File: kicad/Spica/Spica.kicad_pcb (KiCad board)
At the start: 2 copper layers, 61 x 61 mm, 13 parts, among them IC1 TA48033S, M1 Motor_DC, M2 Motor_DC, SW1 SW_SPDT, U1 ESP32-DEVKITC-32D, U2 DRV8835-akizuki, U3 HC-SR04, U4 AE-XCL102D503CR-G

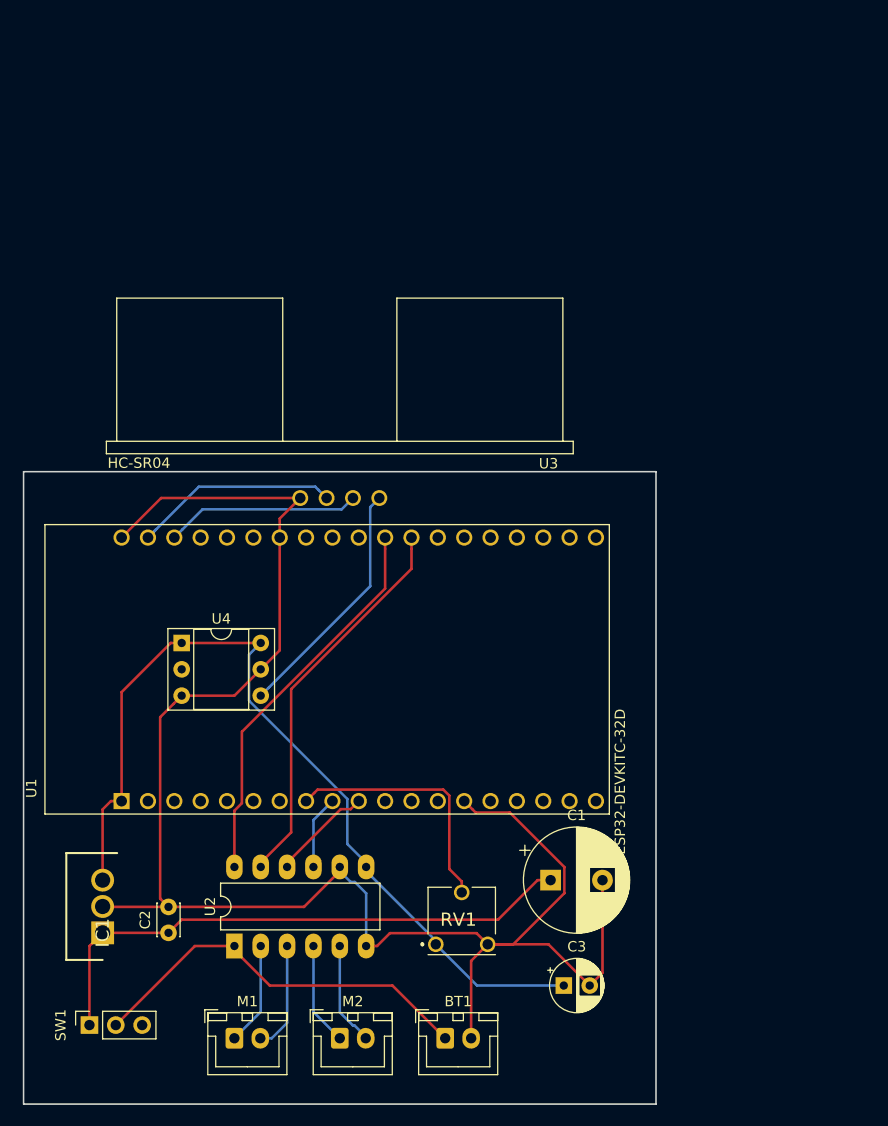
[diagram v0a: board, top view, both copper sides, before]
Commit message: Add surface GND
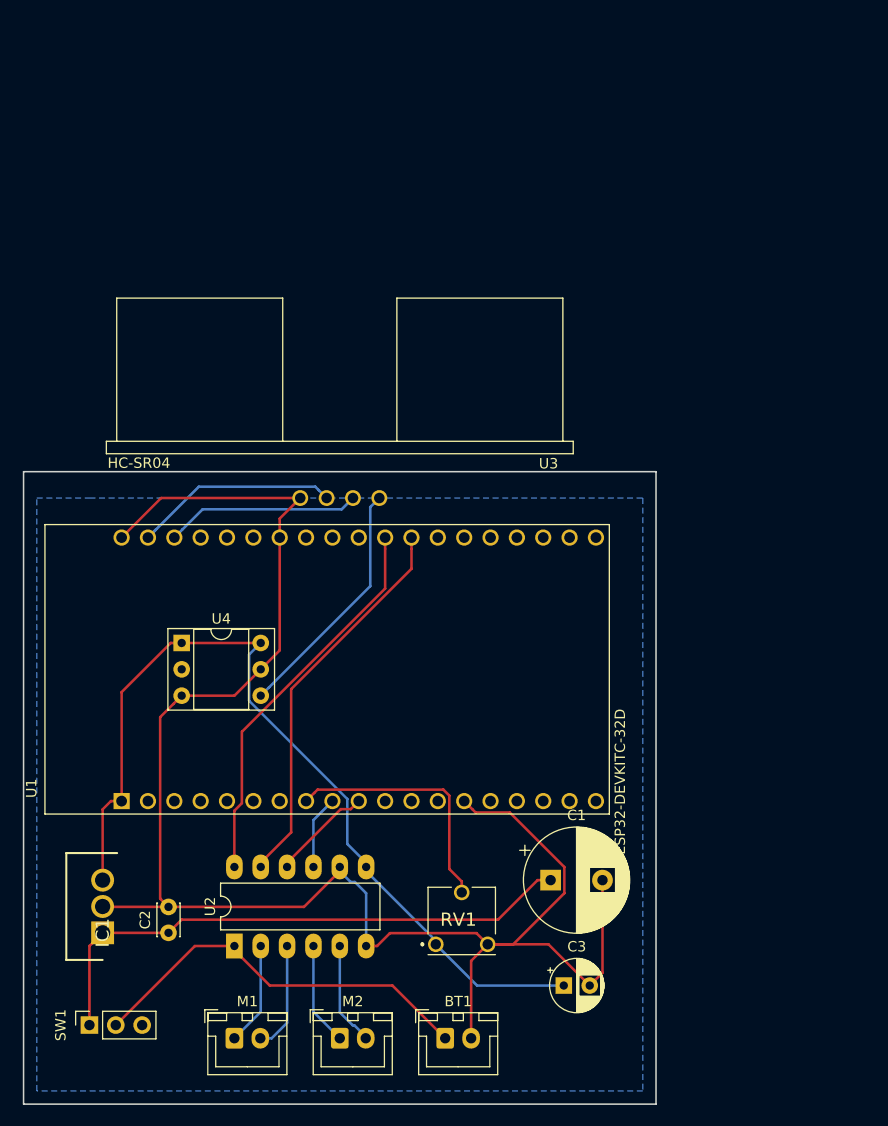
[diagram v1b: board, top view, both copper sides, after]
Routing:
- added copper zone on B.Cu, net GND
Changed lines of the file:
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@@
       (outputformat 1)
       (mirror false)
-      (drillshape 1)
+      (drillshape 0)
       (scaleselection 1)
-      (outputdirectory ""))
+      (outputdirectory "../../../../Downloads/export/"))
   )
   (net 0 "")
@@
   (segment (start 152.795001 92.314999) (end 152.795001 99.934999) (width 0.25) (layer B.Cu) (net 44))
   (segment (start 153.67 91.44) (end 152.795001 92.314999) (width 0.25) (layer B.Cu) (net 44))
+  (zone (net 2) (net_name GND) (layer B.Cu) (hatch edge 0.508)
+    (connect_pads (clearance 0.508))
+    (min_thickness 0.254)
+    (fill yes (arc_segments 16) (thermal_gap 0.508) (thermal_bridge_width 0.508))
+    (polygon
+      (pts
+        (xy 179.07 91.44) (xy 179.07 148.59) (xy 120.65 148.59) (xy 120.65 91.44) (xy 125.73 91.44)
+      )
+    )
+  )
 )

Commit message: ベタパターンを追加
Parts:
- added C4: 0.1μ, Capacitor_THT:C_Disc_D3.0mm_W2.0mm_P2.50mm, F.Cu at (151.1, 99.1)
- added C5: 10μ, Capacitor_THT:CP_Radial_D5.0mm_P2.50mm, F.Cu at (158.8, 102.9)
- added REF**: MountingHole_3.2mm_M3, MountingHole:MountingHole_3.2mm_M3, F.Cu at (196.8, 63.5)
- added REF**: MountingHole_3.2mm_M3, MountingHole:MountingHole_3.2mm_M3, F.Cu at (196.8, 125.7)
- added REF**: MountingHole_3.2mm_M3, MountingHole:MountingHole_3.2mm_M3, F.Cu at (141.0, 125.7)
- added REF**: MountingHole_3.2mm_M3, MountingHole:MountingHole_3.2mm_M3, F.Cu at (141.0, 63.5)
- moved U2 44.4 mm to (177.8, 111.8)
- moved M1 41.0 mm to (175.3, 123.2)
- moved M2 41.0 mm to (185.4, 123.2)
- moved SW1 33.6 mm to (154.9, 125.7), turned to 270 degrees
- moved IC1 32.8 mm to (146.1, 106.7)
- moved U3 32.8 mm to (168.9, 64.8)
- moved U1 32.5 mm to (168.9, 82.5)
- moved C2 31.0 mm to (151.1, 108.0)
- moved U4 30.3 mm to (151.1, 80.0)
- moved C3 26.7 mm to (160.0, 114.3), turned to 180 degrees
- moved RV1 26.5 mm to (168.9, 106.7), turned to 180 degrees
- moved C1 23.3 mm to (148.6, 119.4), turned to 90 degrees
- moved BT1 20.9 mm to (165.1, 123.2)
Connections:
- BT1 pad 1: VCC -> Net-(BT1-Pad1)
- C1 pad 1: Net-(C1-Pad1) -> VCC
- C2 pad 1: Net-(C1-Pad1) -> VCC
- IC1 pad 1: Net-(C1-Pad1) -> VCC
- SW1 pad 1: Net-(C1-Pad1) -> Net-(BT1-Pad1)
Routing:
- net 5V: track 23.8 -> 142.0 mm
- net Net-(C1-Pad1): track 54.7 -> 0.00 mm
- net VCC: track 38.8 -> 61.2 mm
- net IO17: track 37.8 -> 57.5 mm
- net IO16: track 37.8 -> 56.4 mm
- net IO25: track 7.11 -> 23.8 mm
- net Net-(BT1-Pad1): track 0.00 -> 11.2 mm
- net Net-(RV1-Pad2): track 24.3 -> 14.7 mm
- net GND: track 169.5 -> 163.2 mm
- net IO26: track 9.77 -> 15.3 mm
- net 3.3V: track 85.8 -> 90.8 mm
- net Net-(M1-Pad1): track 9.94 -> 14.5 mm
- net Net-(M1-Pad2): track 10.6 -> 14.3 mm
- net IO23: track 20.8 -> 18.1 mm
- net Net-(M2-Pad2): track 10.0 -> 11.8 mm
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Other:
- board size 61 x 61 mm -> 63.5 x 69.8 mm
- net class Default: trace_width 0.25 -> 1.27

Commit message: 細かな修正
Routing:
- added copper zone on F.Cu, net GND
- added copper zone on F.Cu, net Net-(BT1-Pad1)
- added copper zone on F.Cu, net VCC
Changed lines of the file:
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@@
+    )
+  )
+  (zone (net 45) (net_name "Net-(BT1-Pad1)") (layer F.Cu) (hatch edge 0.508)
+    (connect_pads yes (clearance 0.508))
+    (min_thickness 0.254)
+    (fill yes (arc_segments 16) (thermal_gap 0.508) (thermal_bridge_width 0.508) (smoothing fillet) (radius 1))
+    (polygon
+      (pts
+        (xy 154.94 120.65) (xy 154.94 128.27) (xy 165.1 128.27) (xy 165.1 120.65)
+      )
+    )
+  )
+  (zone (net 1) (net_name VCC) (layer F.Cu) (hatch edge 0.508)
+    (connect_pads yes (clearance 0.508))
+    (min_thickness 0.254)
+    (fill yes (arc_segments 16) (thermal_gap 0.508) (thermal_bridge_width 0.508) (smoothing fillet) (radius 1))
+    (polygon
+      (pts
+        (xy 153.67 128.27) (xy 153.67 119.38) (xy 170.18 119.38) (xy 175.26 119.38) (xy 175.26 114.3)
+        (xy 179.07 114.3) (xy 179.07 109.22) (xy 172.72 109.22) (xy 170.18 109.22) (xy 170.18 111.76)
+        (xy 166.37 115.57) (xy 154.94 115.57) (xy 154.94 109.22) (xy 152.4 106.68) (xy 143.51 106.68)
+        (xy 143.51 120.65) (xy 146.05 123.19) (xy 146.05 128.27)
+      )
+    )
+  )
+  (zone (net 2) (net_name GND) (layer F.Cu) (hatch edge 0.508)
+    (connect_pads (clearance 0.508))
+    (min_thickness 0.254)
+    (fill yes (arc_segments 16) (thermal_gap 0.508) (thermal_bridge_width 0.508))
+    (polygon
+      (pts
+        (xy 166.37 129.54) (xy 166.37 120.65) (xy 200.66 120.65) (xy 200.66 121.92) (xy 194.31 121.92)
+        (xy 193.04 123.19) (xy 193.04 129.54)
+      )
     )
   )
